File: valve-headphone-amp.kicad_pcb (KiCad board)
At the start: 2 copper layers, 120 x 66.7 mm, 49 parts, among them J1 RCJ-042, J2 PJ-002AH, J3 SJ1-3533N, J4 RCJ-043, J5 SJ1-3533N, K1 6-1462034-7, Q1 IRF610, Q2 IRF610, Q3 SSN1N45, U1 LM317_TO-220, U2 LM317_TO-220, U3 NE555P

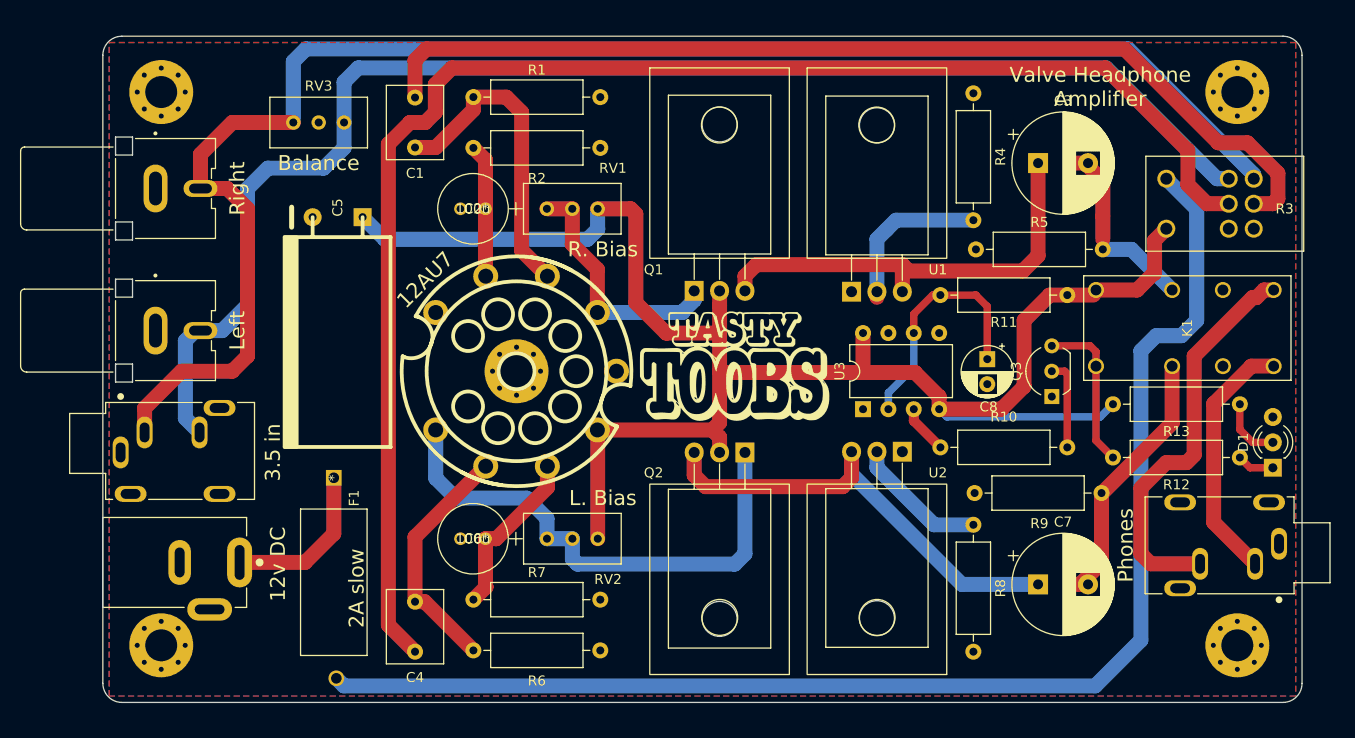
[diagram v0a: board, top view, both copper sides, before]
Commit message: Version with TRRS and media button support
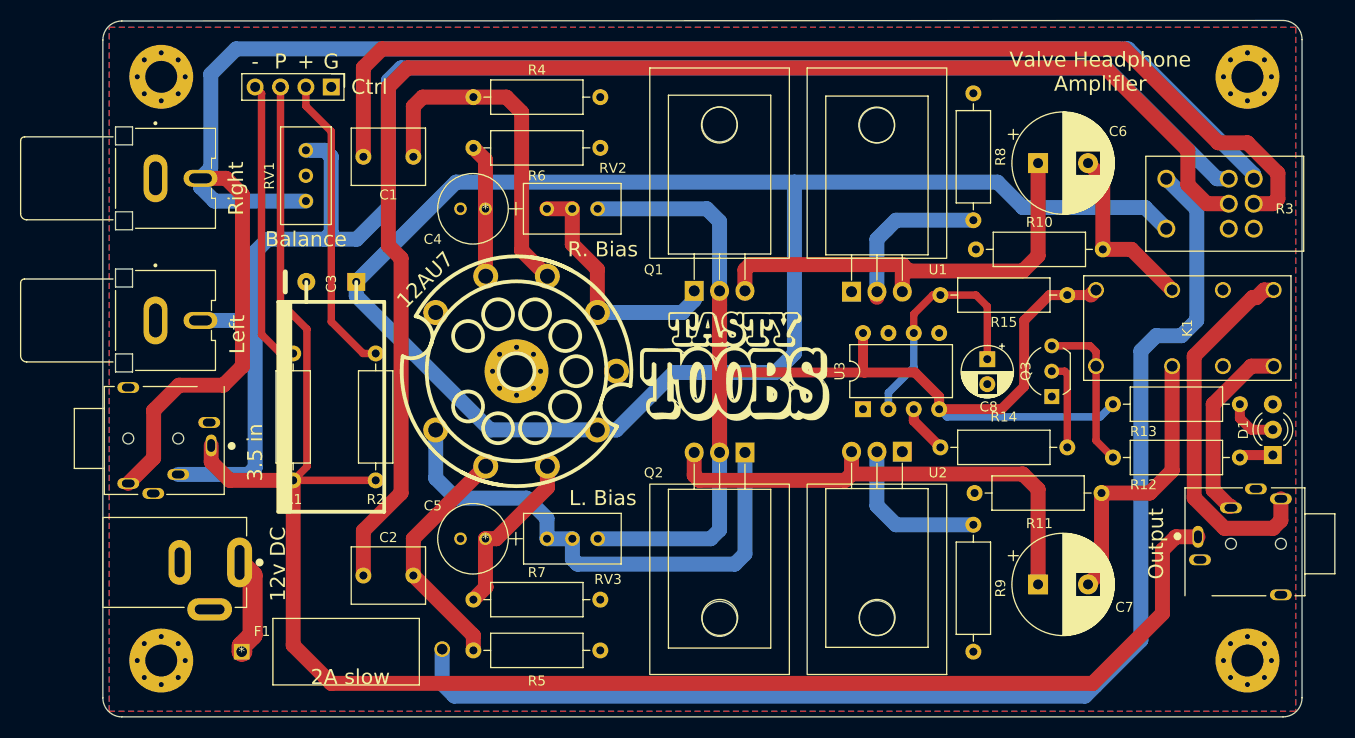
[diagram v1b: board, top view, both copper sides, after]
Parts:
- added J6: SJ-435107, 3:CUI_SJ-435107, F.Cu at (201.9, 91.4)
- added R1: 1k, Resistor_THT:R_Axial_DIN0309_L9.0mm_D3.2mm_P12.70mm_Horizontal, F.Cu at (106.7, 72.4)
- added R2: 1k, Resistor_THT:R_Axial_DIN0309_L9.0mm_D3.2mm_P12.70mm_Horizontal, F.Cu at (114.9, 72.4)
- J3: value SJ1-3533N -> SJ-435107; footprint 3:CUI_SJ1-3533NS -> 3:CUI_SJ-435107
- J5: value SJ1-3533N -> Conn_01x04; footprint 3:CUI_SJ1-3533NS -> Connector_PinHeader_2.54mm:PinHeader_1x04_P2.54mm_Vertical
- moved J3 112.1 mm to (93.8, 80.9), turned to 0 degrees
- moved J5 42.2 mm to (110.5, 45.7), turned to -90 degrees
- moved F1 19.7 mm to (101.5, 102.2), turned to 0 degrees
- moved C2 9.21 mm to (113.7, 94.6), turned to 0 degrees
- moved C1 7.86 mm to (113.7, 52.7), turned to 0 degrees
- moved C3 6.51 mm to (110.5, 65.2)
- moved RV1 4.73 mm to (108.0, 52.1), turned to 90 degrees
- moved H2 1.83 mm to (202.2, 44.7)
- moved H4 1.83 mm to (202.2, 103.1)
- moved H1 1.52 mm to (93.5, 44.7)
- moved H3 1.52 mm to (93.5, 103.1)
- moved D1 1.27 mm to (204.7, 82.6)
- moved J1 1.02 mm to (88.9, 54.9)
- moved J2 1.02 mm to (88.9, 69.1)
- renumbered C4 to C2, C5 to C3, C2 to C4, C6 to C5, C3 to C6, J4 to J2, J2 to J4, R5 to R10, R9 to R11, R10 to R14, R11 to R15, R1 to R4, R6 to R5, R2 to R6, R4 to R8, R8 to R9, RV3 to RV1, RV1 to RV2, RV2 to RV3
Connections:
- J2 pad 2: Net-(J4-Pad2) -> Net-(J2-Pad2)
- J3 pad 1: GND -> Net-(J3-Pad1)
- J3 pad 2: Net-(J3-Pad2) -> Net-(J2-Pad2)
- J3 pad 3: Net-(J3-Pad3) -> GND
- J5 pad 2: Net-(J1-Pad2) -> Net-(J5-Pad2)
- J5 pad 3: Net-(J4-Pad2) -> Net-(J3-Pad1)
- K1 pad 4: Net-(J3-Pad2) -> Net-(J6-Pad2)
- K1 pad 5: Net-(J3-Pad3) -> Net-(J6-Pad4)
- R3 pad R2_3: Net-(J4-Pad2) -> Net-(J2-Pad2)
- RV1 pad 1: Net-(J4-Pad2) -> Net-(J2-Pad2)
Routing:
- net Net-(J3-Pad1): track 0.00 -> 178.3 mm
- net Net-(J2-Pad2): track 0.00 -> 163.6 mm
- net Net-(J4-Pad2): track 140.8 -> 0.00 mm
- net +12V: track 170.7 -> 301.9 mm
- net Net-(J3-Pad3): track 40.2 -> 0.00 mm
- net Net-(J6-Pad4): track 0.00 -> 37.3 mm
- net Net-(J5-Pad2): track 0.00 -> 30.3 mm
- net Net-(J5-Pad4): track 0.00 -> 29.0 mm
- net Net-(J3-Pad2): track 25.3 -> 0.00 mm
- net Net-(J6-Pad2): track 0.00 -> 18.7 mm
- net Net-(J1-Pad2): track 157.6 -> 175.0 mm
- net Net-(C1-Pad1): track 100.5 -> 111.2 mm
- net Net-(F1-Pad2): track 134.0 -> 127.5 mm
- net Net-(F1-Pad1): track 16.2 -> 10.00 mm
- net Net-(C2-Pad1): track 148.4 -> 143.5 mm
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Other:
- board size 120 x 66.7 mm -> 120 x 69.7 mm
- board text added: "+"
- board text added: "-"
- board text added: "Ctrl"
- board text added: "G"
- board text added: "Output"
- board text added: "P"
- board text added: "github.com/buxtronix/toobs"
- board text removed: "Phones"

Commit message: Add media
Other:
- board text added: "+ -"
- board text added: "L"
- board text added: "R"

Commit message: updates
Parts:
- added J4: Conn_01x02, Connector_PinHeader_2.54mm:PinHeader_1x02_P2.54mm_Vertical, F.Cu at (194.3, 102.2)
- renumbered J4 to J5, J5 to J6, J6 to J7
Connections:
- J7 pad 1: Net-(J3-Pad1) -> Net-(J4-Pad2)
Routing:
- net Net-(J4-Pad2): track 0.00 -> 11.5 mm
- net Net-(J3-Pad1): track 178.3 -> 168.0 mm
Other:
- board text added: "Control"
- board text added: "Control Passthru"
- board text removed: "Ctrl"

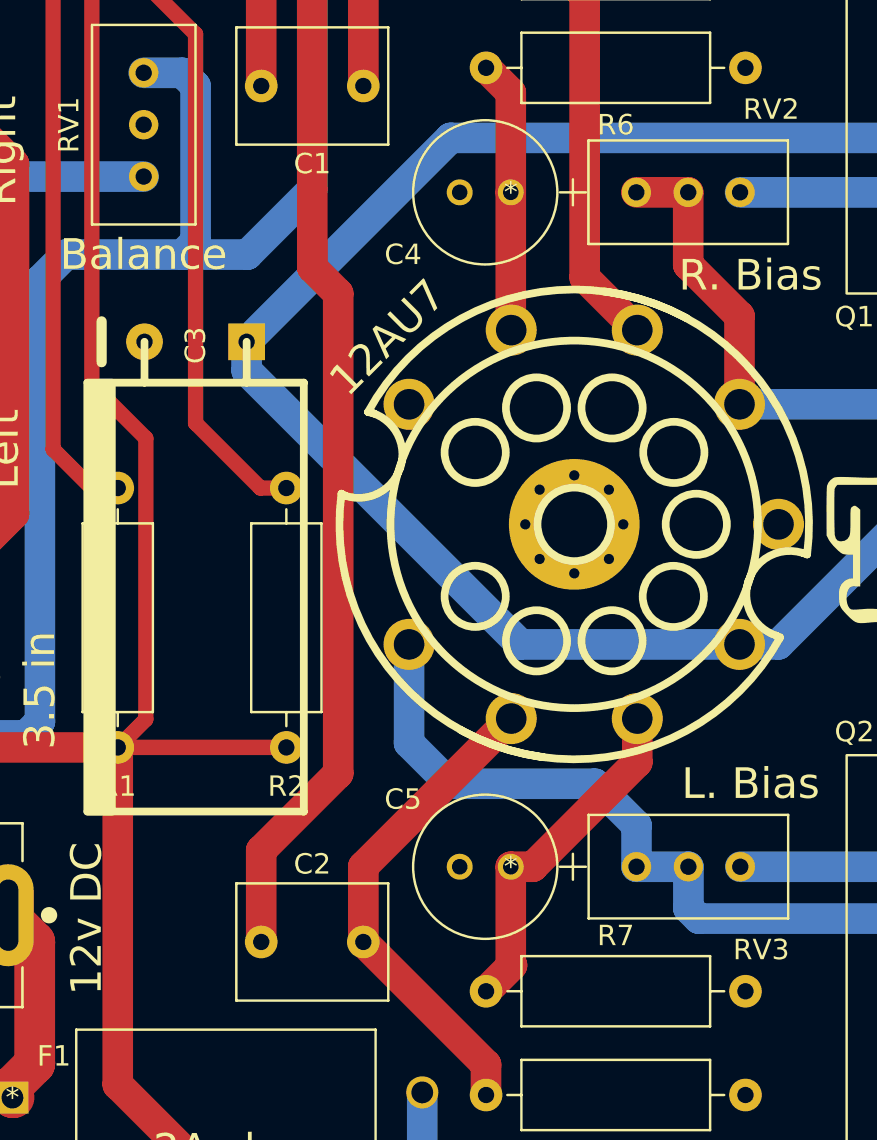
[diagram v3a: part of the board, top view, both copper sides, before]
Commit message: Add LED for glow
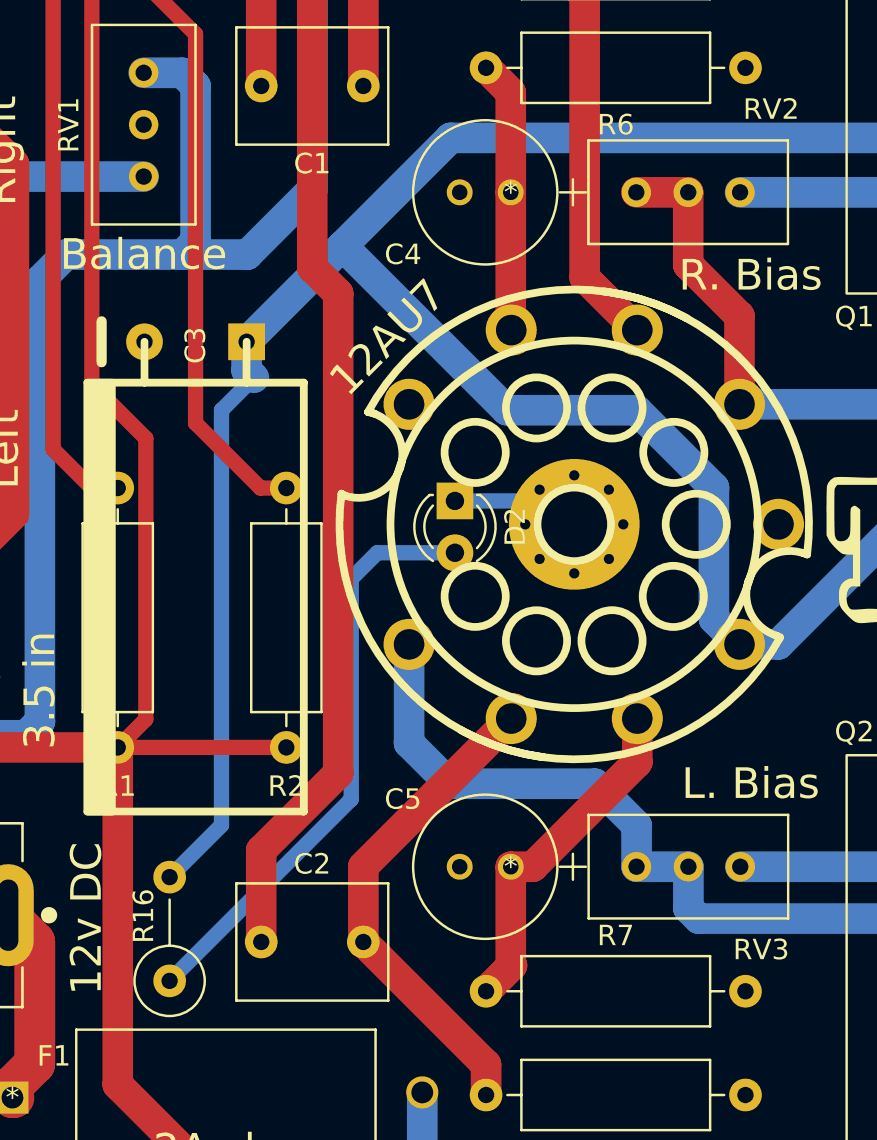
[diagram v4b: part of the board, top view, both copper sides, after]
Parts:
- added D2: LED, LED_THT:LED_D3.0mm_Clear, F.Cu at (123.2, 73.0)
- added R16: 1k, Resistor_THT:R_Axial_DIN0309_L9.0mm_D3.2mm_P5.08mm_Vertical, F.Cu at (109.2, 96.5)
- R1: value 1k -> 470
- R14: value 270 -> 240
- R2: value 1k -> 240
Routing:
- net Net-(D2-Pad2): track 0.00 -> 29.0 mm
- net +12V: track 301.9 -> 330.2 mm
- net GND: track 0.00 -> 4.37 mm

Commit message: update a bit more
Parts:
- removed D2: LED, LED_THT:LED_D3.0mm_Clear
- removed R13: 1k, Resistor_THT:R_Axial_DIN0309_L9.0mm_D3.2mm_P12.70mm_Horizontal
- R15: footprint Resistor_THT:R_Axial_DIN0309_L9.0mm_D3.2mm_P12.70mm_Horizontal -> Resistor_THT:R_Axial_DIN0309_L9.0mm_D3.2mm_P5.08mm_Vertical
- moved D1 75.9 mm to (129.0, 76.7)
- moved R12 34.0 mm to (171.4, 66.7), turned to 0 degrees
- moved H5 15.1 mm to (144.1, 74.3)
- moved K1 13.4 mm to (196.8, 64.6), turned to 0 degrees
- moved R14 12.7 mm to (171.4, 81.9), turned to 0 degrees
- moved G*** 6.63 mm to (157.5, 74.3)
- moved Q3 6.04 mm to (188.6, 77.5), turned to -90 degrees
- moved C8 5.49 mm to (181.0, 75.6), turned to 90 degrees
- moved U3 5.14 mm to (168.8, 78.0)
- moved R15 4.47 mm to (188.6, 66.0), turned to -90 degrees
- moved J4 1.91 mm to (192.4, 102.3)
- moved Q2 0.13 mm to (151.8, 82.3)
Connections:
- C8 pad 1: Net-(C8-Pad1) -> +12V
- C8 pad 2: GND -> Net-(C8-Pad2)
- D1 pad 2: Net-(D1-Pad2) -> GND
- D1 pad 3: GND -> Net-(R16-Pad2)
- R14 pad 1: Net-(Q3-Pad2) -> Net-(R14-Pad1)
- R14 pad 2: Net-(R14-Pad2) -> Net-(Q3-Pad2)
- R15 pad 1: +12V -> Net-(C8-Pad2)
- R15 pad 2: Net-(C8-Pad1) -> GND
- R16 pad 1: Net-(D2-Pad2) -> Net-(R14-Pad1)
- R16 pad 2: +12V -> Net-(R16-Pad2)
- U3 pad 2: Net-(C8-Pad1) -> Net-(C8-Pad2)
- U3 pad 3: Net-(R14-Pad2) -> Net-(R14-Pad1)
- U3 pad 6: Net-(C8-Pad1) -> Net-(C8-Pad2)
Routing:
- net Net-(R14-Pad1): track 0.00 -> 95.8 mm
- net +12V: track 330.2 -> 274.1 mm
- net Net-(D1-Pad1): track 3.40 -> 46.6 mm
- net Net-(J7-Pad4): track 37.3 -> 5.00 mm
- net Net-(C8-Pad2): track 0.00 -> 32.0 mm
- net Net-(K1-Pad1): track 15.2 -> 47.0 mm
- net Net-(R16-Pad2): track 0.00 -> 31.7 mm
- net Net-(D2-Pad2): track 29.0 -> 0.00 mm
- net Net-(C8-Pad1): track 24.5 -> 0.00 mm
- net Net-(C6-Pad2): track 17.9 -> 30.3 mm
- net Net-(J7-Pad2): track 18.7 -> 7.63 mm
- net Net-(D1-Pad2): track 5.18 -> 0.00 mm
- net Net-(R14-Pad2): track 4.92 -> 0.00 mm
- net Net-(J3-Pad1): track 168.0 -> 164.5 mm
- net Net-(Q3-Pad2): track 9.02 -> 5.98 mm
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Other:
- board text added: "Mic/Ctrl Passthru"
- board text removed: "Control Passthru"

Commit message: pcb fab updates
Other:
- board text added: "JLCJLCJLCJLC"
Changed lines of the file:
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@@
       (layerselection 0x00010fc_ffffffff)
       (disableapertmacros false)
-      (usegerberextensions false)
+      (usegerberextensions true)
       (usegerberattributes true)
       (usegerberadvancedattributes true)
@@
       (psa4output false)
       (plotreference true)
-      (plotvalue true)
+      (plotvalue false)
       (plotinvisibletext false)
       (sketchpadsonfab false)
-      (subtractmaskfromsilk false)
+      (subtractmaskfromsilk true)
       (outputformat 1)
       (mirror false)
-      (drillshape 1)
+      (drillshape 0)
       (scaleselection 1)
-      (outputdirectory "")
+      (outputdirectory "gerbers/")
     )
   )
@@
     (effects (font (size 1.5 1.5) (thickness 0.3)) (justify left mirror))
   )
+  (gr_text "JLCJLCJLCJLC" (at 157.48 104.775) (layer "B.SilkS")
+    (effects (font (size 1.2 1.2) (thickness 0.25)) (justify mirror))
+  )
   (gr_text "+   -" (at 102.235 88.9) (layer "B.SilkS")
